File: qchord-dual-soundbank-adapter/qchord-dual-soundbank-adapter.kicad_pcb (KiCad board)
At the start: 2 copper layers, 16 x 33.7 mm, 4 parts, among them SW1 SW_DIP_x01, U1 MX23C8100M, U2 M29F160FB5AN6F2

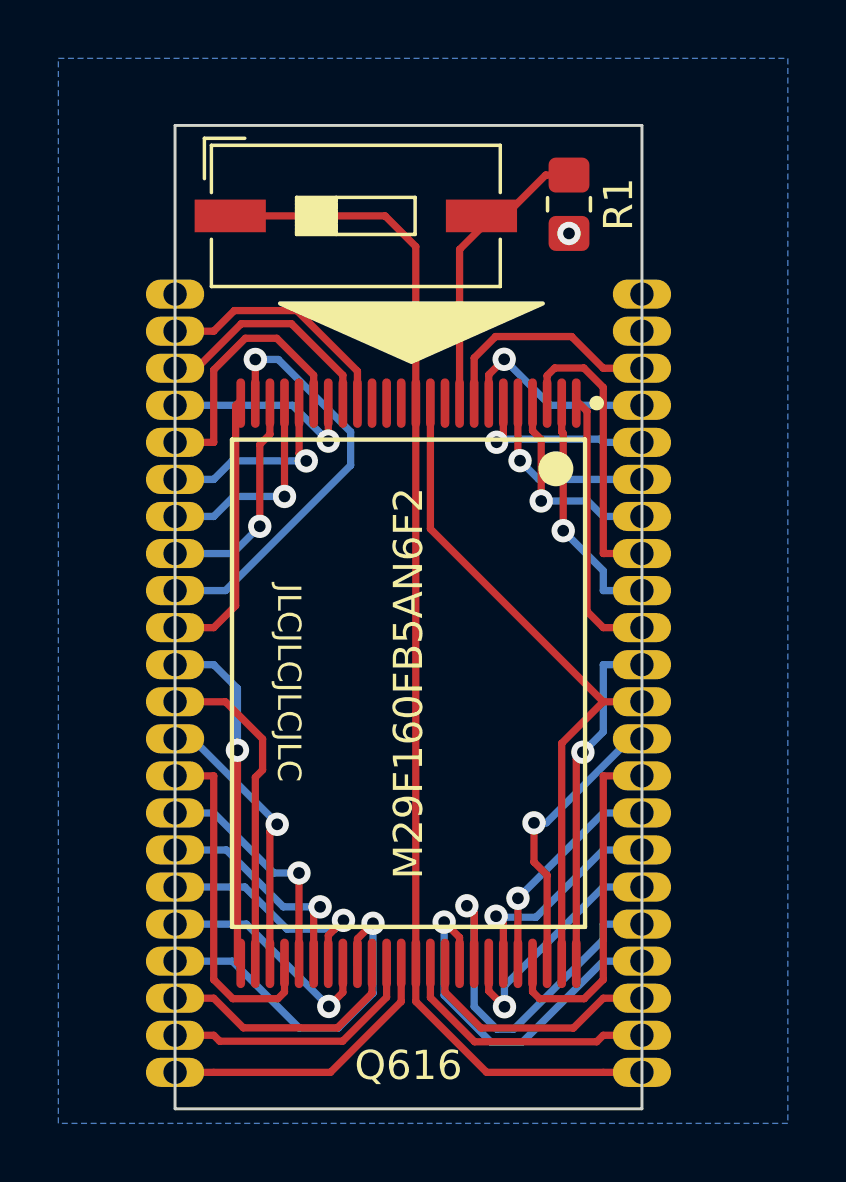
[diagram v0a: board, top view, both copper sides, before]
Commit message: pullup instead of pulldown by default
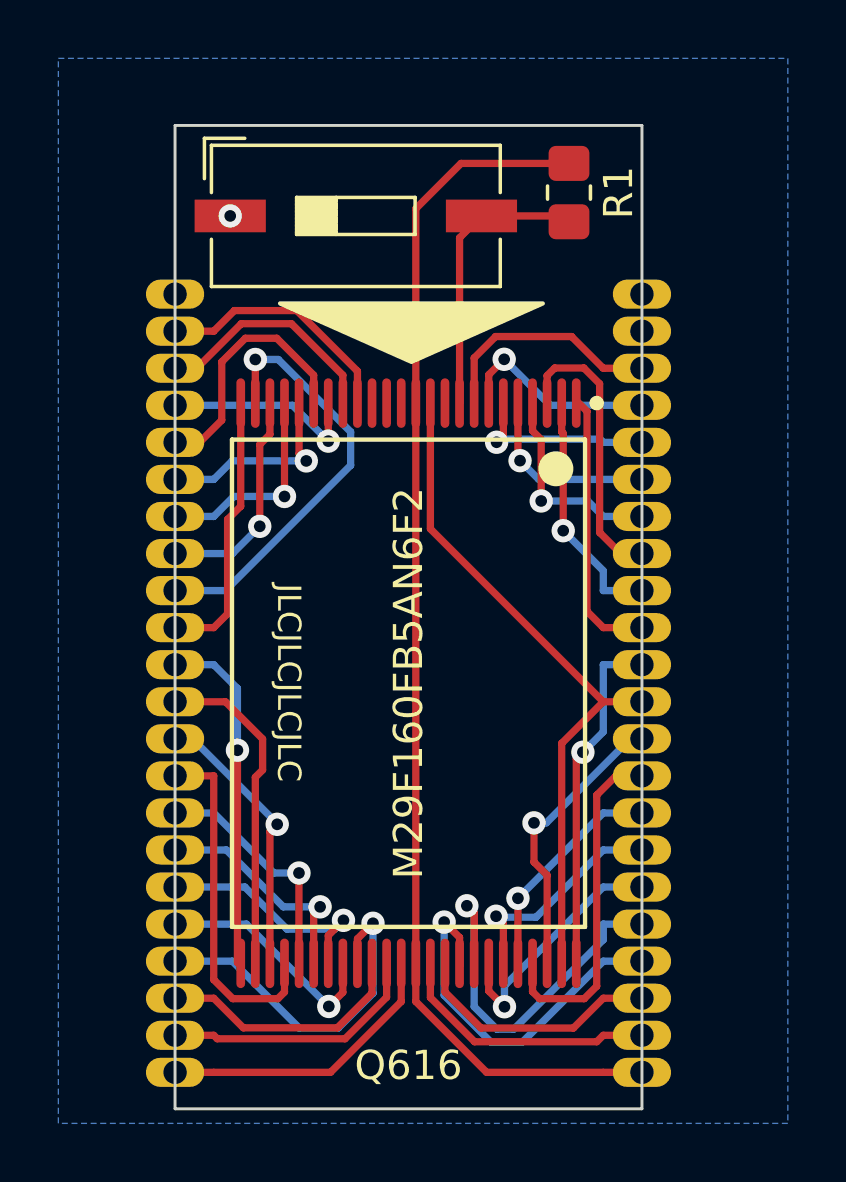
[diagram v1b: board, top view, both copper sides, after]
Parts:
- moved R1 0.40 mm to (100.0, 60.6)
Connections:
- R1 pad 1: GND -> /A19
- R1 pad 2: /A19 -> VCC
- SW1 pad 1: VCC -> GND
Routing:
- net VCC: track 40.4 -> 41.4 mm
